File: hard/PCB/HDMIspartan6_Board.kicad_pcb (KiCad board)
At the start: 2 copper layers, 58.5 x 99 mm, 249 parts, among them P1 CONN_02X20, P2 CONN_02X03, P3 CONN_01X03, P4 CONN_02X05, P5 CONN_02X05, U1 XC6SLX9-2TQG144C, U2 TPS62133RGTR, U3 ZLDO1117G33TA, U4 ZLDO1117G12TA, U5 MAX5864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

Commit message: silkS progresing
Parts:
- removed HDMI1: HDMI_A, Project:HDMI_FCI_10029449-11[13]RLF
- removed LVDS1: CONN_02X09, Project:LVDS_SMD
- removed PW_LCD1: B6B-PH-K-S(LF)(SN), Connectors_JST:JST_PH_B6B-PH-K_06x2.00mm_Straight
- removed RST1: B3SL-1002P, Buttons_Switches_SMD:SW_SPST_KMR2
- added B1: KMR211NG LFS, Buttons_Switches_SMD:SW_SPST_KMR2, F.Cu at (150.0, 57.7)
- added J1: CONN_02X09, Project:LVDS_SMD, F.Cu at (155.9, 126.6)
- added J2: B6B-PH-K-S(LF)(SN), Connectors_JST:JST_PH_B6B-PH-K_06x2.00mm_Straight, F.Cu at (148.0, 148.1)
- added J3: HDMI_A, Project:HDMI_FCI_10029449-11[13]RLF, F.Cu at (158.9, 88.7)
- moved JMS1 5.96 mm to (162.5, 143.4)
- moved TH80 5.96 mm to (126.5, 118.0)
- moved XF2 5.96 mm to (126.5, 73.5)
- moved C12 5.96 mm to (125.2, 95.1)
- moved C14 5.96 mm to (141.7, 100.2)
- moved C16 5.96 mm to (129.0, 100.2)
- moved C19 5.96 mm to (123.3, 86.2)
- moved C26 5.96 mm to (145.5, 95.1)
- moved C27 5.96 mm to (139.2, 104.0)
- moved C29 5.96 mm to (131.6, 104.0)
- moved C37 5.96 mm to (141.7, 95.1)
- moved C39 5.96 mm to (144.3, 82.4)
- moved C40 5.96 mm to (125.2, 104.0)
- moved C43 5.96 mm to (117.6, 70.4)
- moved C44 5.96 mm to (116.3, 70.4)
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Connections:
- FT1 pad 1: (no net) -> Net-(FT1-Pad1)
- FT1 pad 11: (no net) -> Net-(FT1-Pad11)
- FT1 pad 12: (no net) -> Net-(FT1-Pad12)
- FT1 pad 13: (no net) -> Net-(FT1-Pad13)
- FT1 pad 15: (no net) -> Net-(FT1-Pad15)
- FT1 pad 16: (no net) -> Net-(FT1-Pad16)
- FT1 pad 17: (no net) -> Net-(FT1-Pad17)
- FT1 pad 19: (no net) -> Net-(FT1-Pad19)
- FT1 pad 20: (no net) -> Net-(FT1-Pad20)
- FT1 pad 27: (no net) -> Net-(FT1-Pad27)
- FT1 pad 28: (no net) -> Net-(FT1-Pad28)
- FT1 pad 29: (no net) -> Net-(FT1-Pad29)
- FT1 pad 30: (no net) -> Net-(FT1-Pad30)
- FT1 pad 32: (no net) -> Net-(FT1-Pad32)
- FT1 pad 33: (no net) -> Net-(FT1-Pad33)
- FT1 pad 35: (no net) -> Net-(FT1-Pad35)
- FT1 pad 36: (no net) -> Net-(FT1-Pad36)
- FT1 pad 37: (no net) -> Net-(FT1-Pad37)
- FT1 pad 38: (no net) -> Net-(FT1-Pad38)
- FT1 pad 41: (no net) -> Net-(FT1-Pad41)
- FT1 pad 48: (no net) -> Net-(FT1-Pad48)
- JMS1 pad 4: (no net) -> Net-(JMS1-Pad4)
- JMS2 pad 4: (no net) -> Net-(JMS2-Pad4)
- P1 pad 1: (no net) -> Net-(P1-Pad1)
- P1 pad 17: (no net) -> Net-(P1-Pad17)
- P2 pad 5: (no net) -> Net-(P2-Pad5)
- U1 pad 102: (no net) -> Net-(U1-Pad102)
- U1 pad 104: (no net) -> Net-(U1-Pad104)
- U1 pad 11: (no net) -> Net-(U1-Pad11)
- U1 pad 118: (no net) -> Net-(U1-Pad118)
- U1 pad 119: (no net) -> Net-(U1-Pad119)
- U1 pad 120: (no net) -> Net-(U1-Pad120)
- U1 pad 22: (no net) -> Net-(U1-Pad22)
- U1 pad 23: (no net) -> Net-(U1-Pad23)
- U1 pad 55: (no net) -> Net-(U1-Pad55)
- U1 pad 56: (no net) -> Net-(U1-Pad56)
- U1 pad 57: (no net) -> Net-(U1-Pad57)
- U1 pad 58: (no net) -> Net-(U1-Pad58)
- U1 pad 66: (no net) -> Net-(U1-Pad66)
- U1 pad 67: (no net) -> Net-(U1-Pad67)
- U1 pad 72: (no net) -> Net-(U1-Pad72)
- U1 pad 88: (no net) -> Net-(U1-Pad88)
- U1 pad 98: (no net) -> Net-(U1-Pad98)
- U1 pad 99: (no net) -> Net-(U1-Pad99)
- U5 pad 38: (no net) -> Net-(U5-Pad38)
- U7 pad 12: (no net) -> Net-(U7-Pad12)
- U7 pad 22: (no net) -> /atmega32u4/uD5
- U7 pad 25: (no net) -> /atmega32u4/uD4
- U7 pad 26: (no net) -> /atmega32u4/uD6
- U7 pad 30: (no net) -> /atmega32u4/uD8
- XS2 pad 1: (no net) -> Net-(XS2-Pad1)
- XS2 pad 8: (no net) -> Net-(XS2-Pad8)
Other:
- net class Default: clearance 0.2 -> 0.1
- net class Vcc: clearance 0.2 -> 0.1
- rule trace_clearance: 0.2 -> 0.1
- board text added: "1"
- board text added: "GPIO"
- board text added: "HDMI"
- board text added: "LVDS"
- board text added: "MICRO SD CARD"
- board text added: "PW_LCD"
- board text added: "RST"
- board text added: "USB1"
- board text added: "USB2"

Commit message: SilkS 2
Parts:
- added G***: LOGO, Project:uECCI_Logo_silkS, F.Cu at (152.6, 119.8)
- added G***: LOGO, Project:Logo_silk_polarity_center_5x1.4mm, F.Cu at (194.6, 120.1)
- added REF***: OSHW-Symbol_6.7x6mm_SilkScreen, Symbols:OSHW-Symbol_6.7x6mm_SilkScreen, F.Cu at (130.3, 90.2)
- added REF***: ESD-Logo_6.6x6mm_SilkScreen, Symbols:ESD-Logo_6.6x6mm_SilkScreen, F.Cu at (172.6, 77.4)
- added REF***: WEEE-Logo_4.2x6mm_SilkScreen, Symbols:WEEE-Logo_4.2x6mm_SilkScreen, F.Cu at (193.4, 112.3)
- moved TH27 85.8 mm to (194.3, 129.9), turned to 90 degrees
- moved TH22 83.3 mm to (196.2, 123.0), turned to 90 degrees
- moved TH1 81.8 mm to (190.5, 130.6), turned to 270 degrees
- moved TH24 80.2 mm to (196.2, 77.2), turned to 90 degrees
- moved TH29 79.8 mm to (196.2, 116.6), turned to 90 degrees
- moved TH39 77.9 mm to (196.2, 82.4), turned to 90 degrees
- moved TH38 77.6 mm to (196.2, 111.5), turned to 90 degrees
- moved TH109 76.3 mm to (196.2, 87.4), turned to 90 degrees
- moved TH30 76.1 mm to (196.2, 106.4), turned to 90 degrees
- moved TH93 76.0 mm to (99.1, 128.0), turned to 90 degrees
- moved TH108 75.2 mm to (196.2, 93.7), turned to 90 degrees
- moved TH110 75.1 mm to (196.2, 100.1), turned to 90 degrees
- moved RS7 74.7 mm to (194.3, 84.2), turned to 0 degrees
- moved LED2 74.0 mm to (194.3, 86.1), turned to 0 degrees
- moved PS1 73.5 mm to (185.6, 127.4), turned to 90 degrees
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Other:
- board size 58.5 x 99 mm -> 99 x 58.5 mm
- board text added: "-"
- board text added: "3V3"
- board text added: "5V"
- board text added: "6V"
- board text added: "@fabeltranm"
- board text added: "A00"
- board text added: "A01"
- board text added: "A04"
- board text added: "A05"
- board text added: "A06"
- board text added: "A07"
- board text added: "A11"
- board text added: "A12"
- board text added: "ADC-DAC"
- board text added: "ANALOG IN"
- board text added: "C1N"
- board text added: "C1P"
- board text added: "C2N"
- board text added: "C2P"
- board text added: "C3N"
- board text added: "C3P"
- board text added: "C4N"
- board text added: "C4P"
- board text added: "CKN"
- board text added: "CKP"
- board text added: "CS"
- board text added: "DESIGNED IN COLOMBIA"
- board text added: "G04"
- board text added: "G05"
- board text added: "G06"
- board text added: "G08"
- board text added: "G12"
- board text added: "G13"
- board text added: "G16"
- board text added: "G17"
- board text added: "G18"
- board text added: "G19"
- board text added: "G20"
- board text added: "G21"
- board text added: "G23"
- board text added: "G26"
- board text added: "G27"
- board text added: "GND"
- board text added: "HDMI IN"
- board text added: "IA+"
- board text added: "IA-"
- board text added: "ID+"
- board text added: "ID-"
- board text added: "JACK"
- board text added: "M1"
- board text added: "MISO"
- board text added: "MOSI"
- board text added: "MS"
- board text added: "NC"
- board text added: "POWER"
- board text added: "PWR"
- board text added: "QA+"
- board text added: "QA-"
- board text added: "QD+"
- board text added: "QD-"
- board text added: "QUACHO BASIC AT"
- board text added: "RXD"
- board text added: "Rpi"
- board text added: "S"
- board text added: "SCK"
- board text added: "SCL"
- board text added: "SDA"
- board text added: "TXD"
- board text added: "U1"
- board text added: "U5"
- board text added: "USB"
- board text added: "V1.0/2017"
- board text added: "VCC"
- board text removed: "HDMI"

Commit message: SilkS 2.1
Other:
- board text added: "ZONA SUGERIDA PARA EL ARTE INSPIRADO EN K3os"
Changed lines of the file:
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@@
     (links 618)
     (no_connects 0)
-    (area 97.81096 66.44882 256.244758 137.523071)
+    (area 98.363959 73.303879 197.513961 131.953881)
     (thickness 1.6)
-    (drawings 165)
+    (drawings 172)
     (tracks 4419)
     (zones 0)
@@
     (31 B.Cu signal hide)
     (32 B.Adhes user)
-    (33 F.Adhes user)
+    (33 F.Adhes user hide)
     (34 B.Paste user)
-    (35 F.Paste user)
+    (35 F.Paste user hide)
     (36 B.SilkS user)
-    (37 F.SilkS user)
+    (37 F.SilkS user hide)
     (38 B.Mask user)
     (39 F.Mask user)
@@
     (aux_axis_origin 20 90)
     (grid_origin 108.037 156.932)
-    (visible_elements 7FFEFFFF)
+    (visible_elements 7FFEBFDF)
     (pcbplotparams
       (layerselection 0x013ff_80000001)
@@
       (xy 1.530863 -2.420002) (xy 1.583231 -2.473048) (xy 2.125049 -3.022233) (xy 2.12443 -2.935152)) (layer F.SilkS) (width 0.01))
   )
+  (gr_text "ZONA SUGERIDA \nPARA EL ARTE\nINSPIRADO EN K3os" (at 179.48974 105.43604) (layer Dwgs.User)
+    (effects (font (size 0.8 1.5) (thickness 0.2)))
+  )
+  (gr_line (start 161.08744 112.99254) (end 161.08744 92.10104) (angle 90) (layer Dwgs.User) (width 0.1))
+  (gr_line (start 165.79914 112.99254) (end 161.08744 112.99254) (angle 90) (layer Dwgs.User) (width 0.1))
+  (gr_line (start 165.79914 133.79514) (end 165.79914 112.99254) (angle 90) (layer Dwgs.User) (width 0.1))
+  (gr_line (start 198.69214 133.79514) (end 165.79914 133.79514) (angle 90) (layer Dwgs.User) (width 0.1))
+  (gr_line (start 198.69214 91.65654) (end 198.69214 133.79514) (angle 90) (layer Dwgs.User) (width 0.1))
+  (gr_line (start 161.35414 91.65654) (end 198.69214 91.65654) (angle 90) (layer Dwgs.User) (width 0.1))
   (gr_text C1N (at 178.34166 92.63952) (layer F.SilkS)
     (effects (font (size 0.8 0.6) (thickness 0.12)))
@@
   )
   (gr_text 3V3 (at 178.58296 98.60344) (layer F.SilkS)
-    (effects (font (size 0.8 0.8) (thickness 0.12)))
+    (effects (font (size 0.8 0.6) (thickness 0.12)))
   )
   (gr_text A00 (at 105.53256 120.41442 90) (layer B.SilkS)

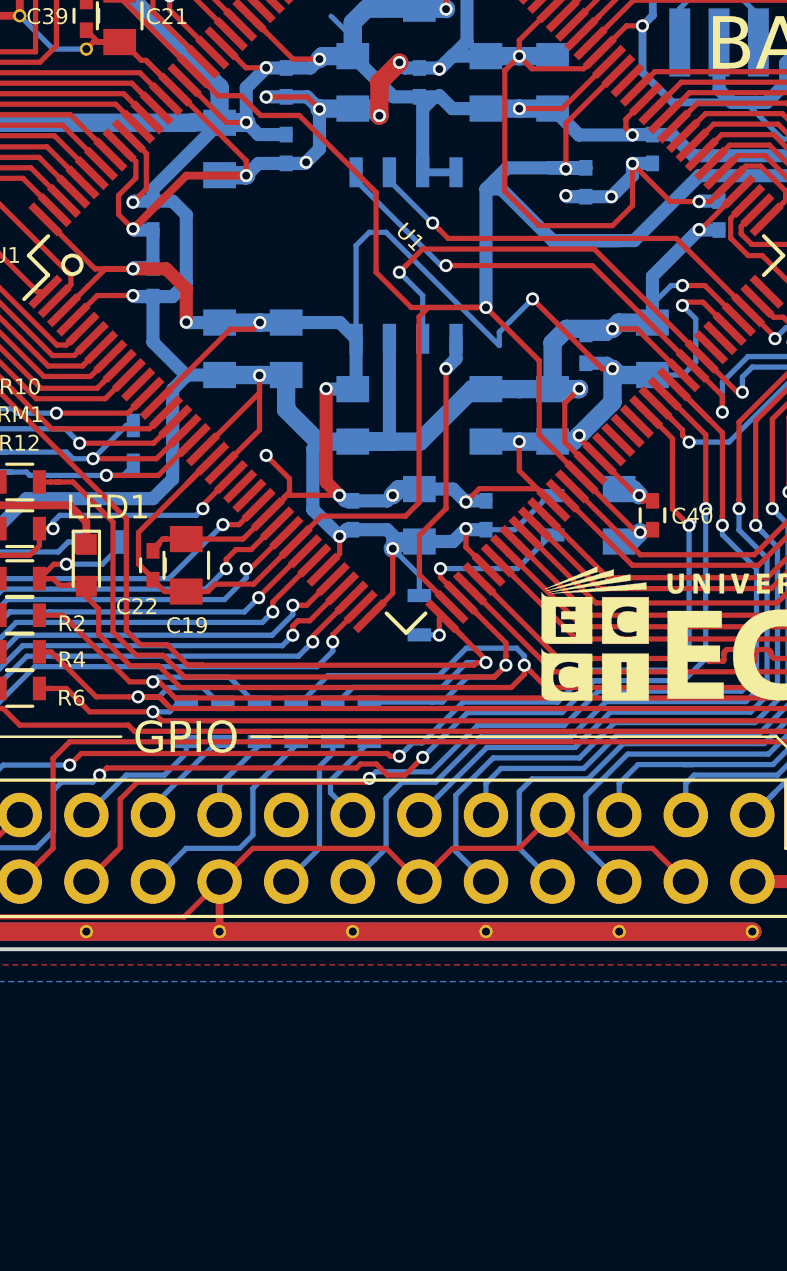
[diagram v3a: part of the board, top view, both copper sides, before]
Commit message: cambio de la memoria flash, referecnia y encapsulado
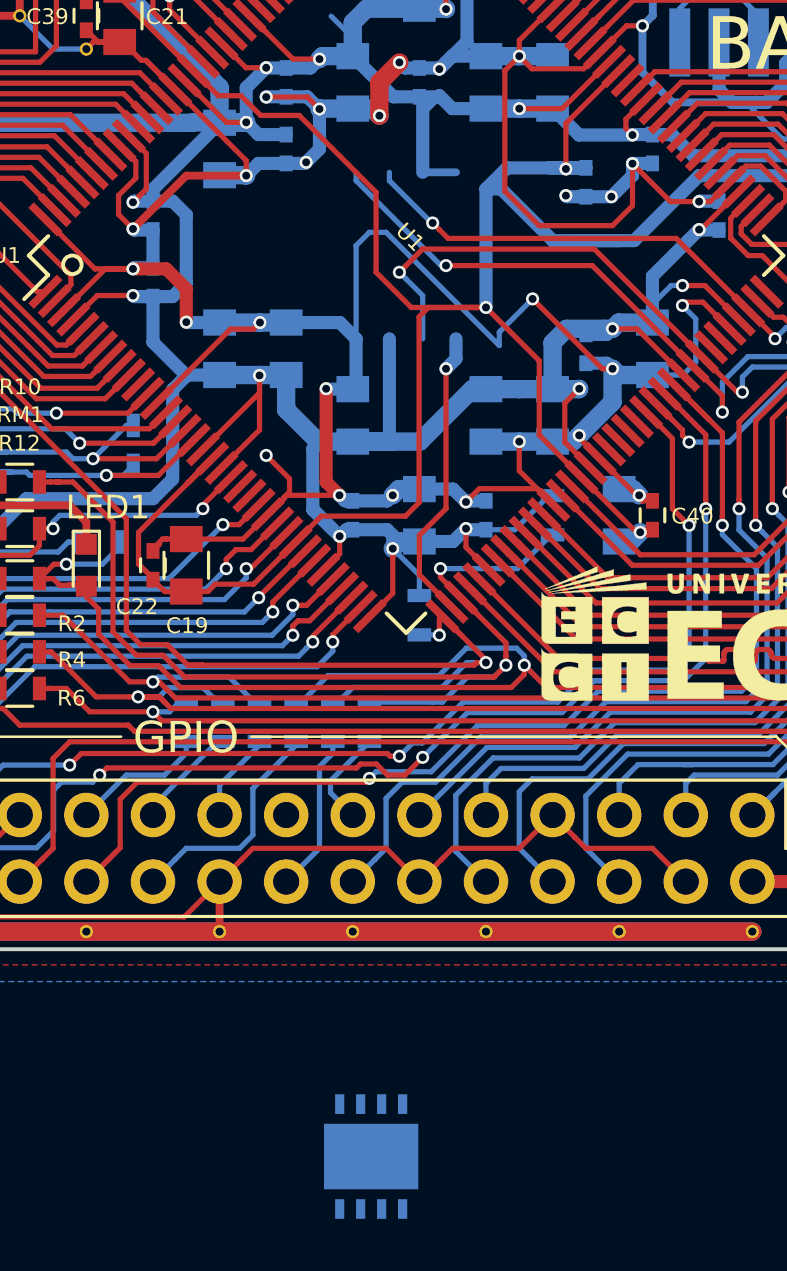
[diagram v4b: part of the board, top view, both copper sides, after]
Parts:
- U6: value S25FL064LABMFI013 -> S25FL064LABNFI041; footprint SMD_Packages:SOIC-8-N -> Housings_DFN_QFN:DFN-8-1EP_4x4mm_Pitch0.8mm
- moved U6 34.4 mm to (139.2, 139.8), turned to 90 degrees

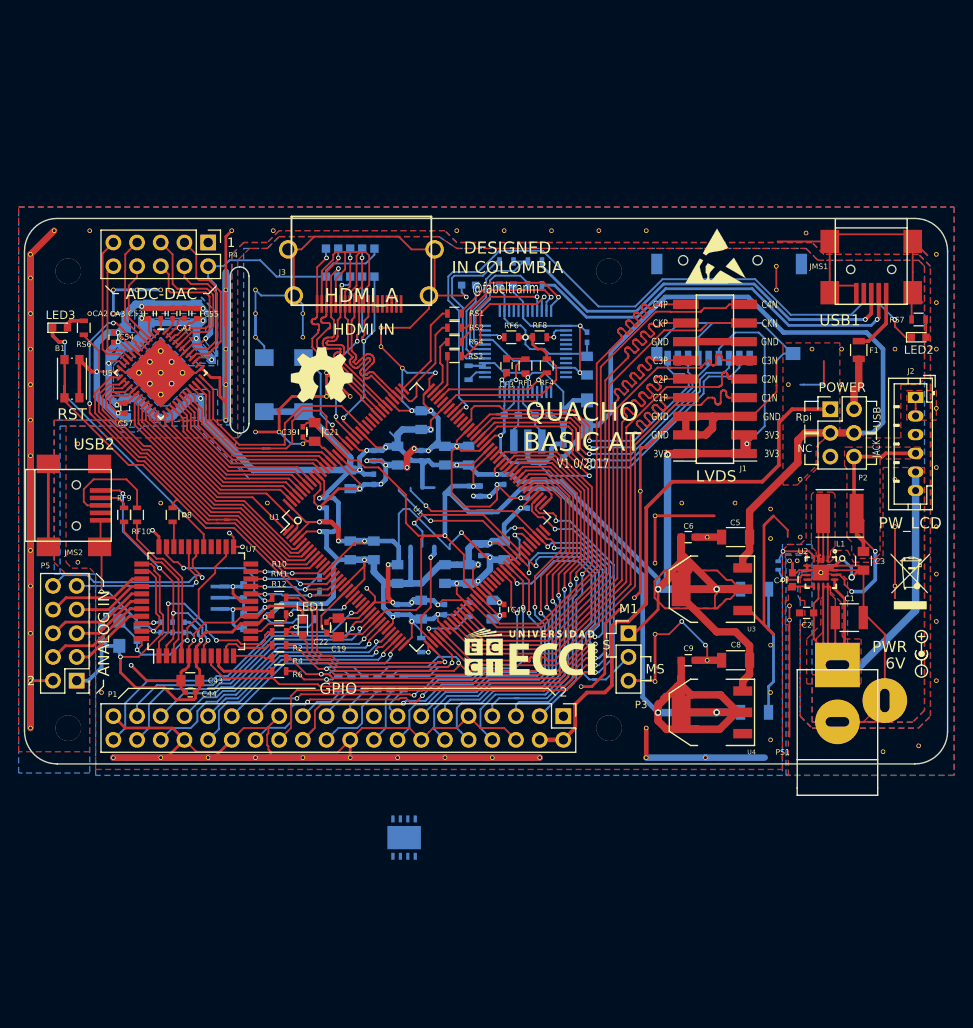
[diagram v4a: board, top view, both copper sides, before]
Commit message: conexión de la memoria flash y verificación del plano de tierras
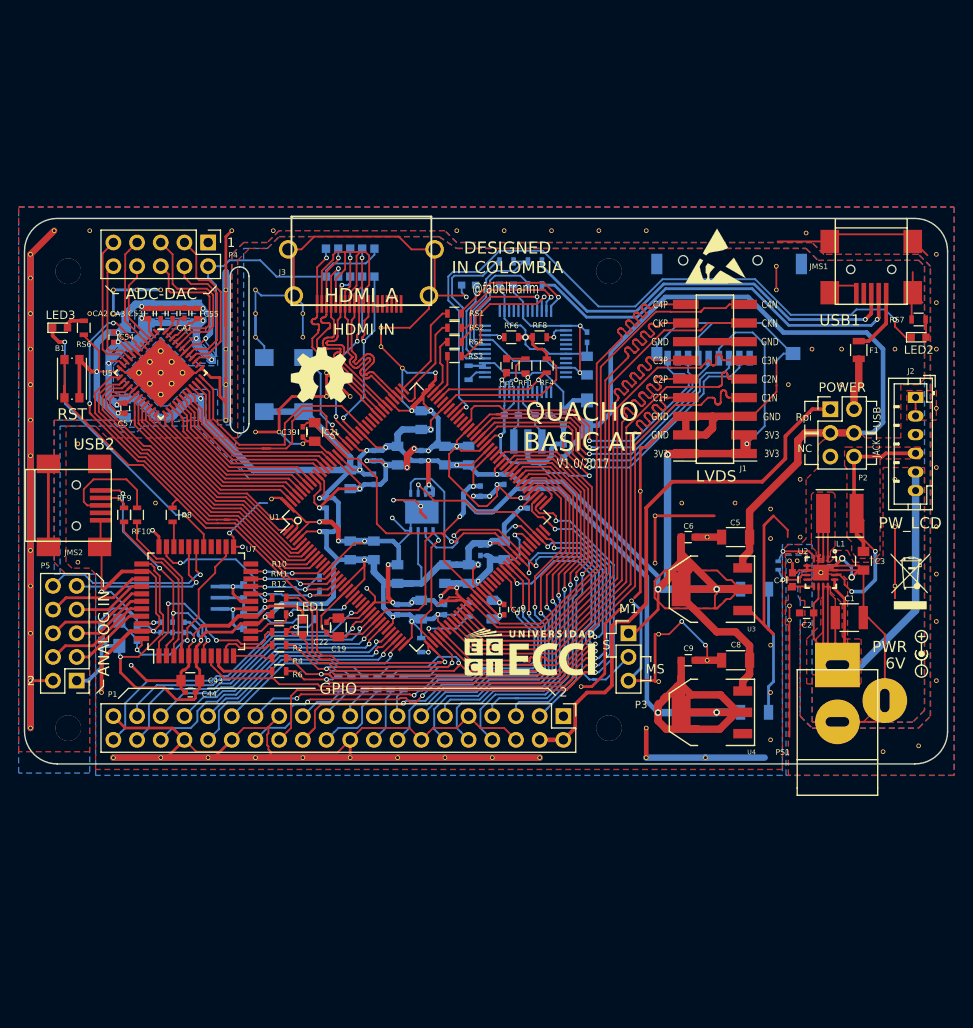
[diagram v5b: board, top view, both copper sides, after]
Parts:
- moved U6 35.0 mm to (141.1, 104.9)
- moved TH52 0.62 mm to (124.9, 103.5)
- moved TH97 0.57 mm to (112.5, 103.9)
- moved TH80 0.45 mm to (163.5, 114.4), turned to 180 degrees
- moved TH10 0.39 mm to (166.5, 123.0)
- moved TH41 0.39 mm to (166.5, 118.0)
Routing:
- net GND: track 1253.5 -> 1292.0 mm
- net +1V2: track 184.5 -> 178.2 mm
- net (no net): track 5.08 -> 0.00 mm
- net /spartan6/Dout: track 77.2 -> 80.8 mm
- net /spartan6/RpID_SD: track 40.6 -> 43.3 mm
- net /spartan6/RpID_SC: track 45.2 -> 47.6 mm
- net /spartan6/Din: track 77.2 -> 74.9 mm
- net /spartan6/sCS: track 11.3 -> 13.5 mm
- net +3V3: track 583.5 -> 582.2 mm, vias 32 -> 34
- net VccRpi: track 59.8 -> 58.5 mm
- net /atmega32u4/ADC11: track 21.1 -> 20.2 mm
- net /spartan6/RpINIT_B: track 3.77 -> 3.12 mm
- net /spartan6/LED2: track 30.6 -> 31.1 mm
